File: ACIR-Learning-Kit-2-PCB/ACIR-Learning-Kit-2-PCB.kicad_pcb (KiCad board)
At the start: 2 copper layers, 297 x 210 mm, 39 parts, among them J1 1S 1P +ve, J10 1S 1P +ve, J11 1S 1P -ve, J12 1S 3P +ve, J13 1S 3P -ve, J14 1S 4P +ve, J15 1S 4P -ve, J16 1S 2P +ve, J17 1S 2P -ve, J18 1S 1P -ve, J19 2S 1P -ve, J2 1S 1P -ve, J20 3S 1P -ve, J3 4S B +ve, J4 4S B -ve, J5 4P B +ve, J6 4P B -ve, J7 2S 1P +ve, J8 3S 1P +ve, J9 4S 1P +ve

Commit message: feat: add PCB design files for ACIR Learning Kits 1 and 2
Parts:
- removed BT1: BH-18650-B5BA008, footprints:BH18650B1BA002
- removed J5: 4P B +ve, TestPoint:TestPoint_Pad_D2.0mm
- removed J6: 4P B -ve, TestPoint:TestPoint_Pad_D2.0mm
- added J21: 1S 1P +ve, TestPoint:TestPoint_Pad_D2.0mm, F.Cu at (169.1, 92.5)
- added J22: 1S 1P -ve, TestPoint:TestPoint_Pad_D2.0mm, F.Cu at (227.1, 92.5)
- added J23: 1S 1P +ve, TestPoint:TestPoint_Pad_D2.0mm, F.Cu at (183.3, 100.2)
- added J24: 1S 1P -ve, TestPoint:TestPoint_Pad_D2.0mm, F.Cu at (219.8, 100.2)
- moved J2 4.89 mm to (145.3, 82.4)
- moved J1 4.89 mm to (249.7, 82.4)
- turned BT7 to 180 degrees
- turned BT9 to 180 degrees
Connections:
- BT6 pad 1: /4P_B+ -> Net-(BT6-+)
- BT6 pad 2: /4P_B- -> Net-(BT6--)
- BT7 pad 1: /4P_B+ -> Net-(BT6--)
- BT7 pad 2: /4P_B- -> Net-(BT7--)
- BT8 pad 1: /4P_B+ -> Net-(BT7--)
- BT8 pad 2: /4P_B- -> Net-(BT8--)
- BT9 pad 1: /4P_B+ -> Net-(BT8--)
- BT9 pad 2: /4P_B- -> Net-(BT9--)
- J1 pad 1: /1S_B+ -> Net-(J1-Pin_1)
- J10 pad 1: /4P_B+ -> Net-(BT6-+)
- J11 pad 1: /4P_B- -> Net-(BT6--)
- J12 pad 1: /4P_B+ -> Net-(BT7--)
- J13 pad 1: /4P_B- -> Net-(BT8--)
- J14 pad 1: /4P_B+ -> Net-(BT9--)
- J15 pad 1: /4P_B- -> Net-(BT8--)
- J16 pad 1: /4P_B+ -> Net-(BT7--)
- J17 pad 1: /4P_B- -> Net-(BT6--)
- J2 pad 1: /1S_B- -> Net-(J1-Pin_1)
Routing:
- net /4P_B-: track 478.6 -> 0.00 mm, vias 797 -> 0
- net /4P_B+: track 478.6 -> 0.00 mm, vias 797 -> 0
- net Net-(J1-Pin_1): track 0.00 -> 208.7 mm, vias 0 -> 242
- net Net-(BT8--): track 0.00 -> 143.9 mm, vias 0 -> 266
- net Net-(BT6--): track 0.00 -> 143.9 mm, vias 0 -> 349
- net Net-(BT7--): track 0.00 -> 113.0 mm, vias 0 -> 319
- net /1S_B-: track 72.0 -> 0.00 mm, vias 121 -> 0
- net /1S_B+: track 72.0 -> 0.00 mm, vias 121 -> 0
- net Net-(BT9--): track 0.00 -> 72.0 mm, vias 0 -> 133
- net Net-(BT6-+): track 0.00 -> 72.0 mm, vias 0 -> 133
- net Net-(J21-Pin_1): track 0.00 -> 57.9 mm
- net Net-(J23-Pin_1): track 0.00 -> 36.4 mm
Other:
- board text added: "4S 1P - (I)"
- board text added: "4S 1P - (II)"
- board text added: "NOTE: In this section the Cells have diffrent ACIR The track Resistance are same but ACIR is diffrent because of the Cell Having Diffrent ACIR"
- board text added: "P1"
- board text added: "P2"
- board text added: "PCB Track Resistance"
- board text added: "Product ID: TST-ACR-V1.1-2607 Sub product ID: TST-ACR-V1.1-L2-2607 Version: V1.1"
- board text removed: "1S 1P"
- board text removed: "1S 4P"
- board text removed: "4S 1P"
- board text removed: "BT1"
- board text removed: "Product ID: TST-ACR-V1.1-2607 Sub product ID: TST-ACR-V1.1-L1-2607 Version: V1.1"

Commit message: feat: add ACIR Learning Kit 2 PCB design files and production outputs
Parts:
- renumbered J2 to P1, J1 to P2, J21 to P3, J22 to P4, J23 to P5, J24 to P6
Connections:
- J13 pad 1: Net-(BT8--) -> Net-(BT6--)
- J14 pad 1: Net-(BT9--) -> Net-(BT7--)
- J16 pad 1: Net-(BT7--) -> Net-(BT9--)
- J17 pad 1: Net-(BT6--) -> Net-(BT8--)
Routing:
- net Net-(BT6--): track 143.9 -> 270.9 mm, vias 349 -> 25
- net Net-(J21-Pin_1): track 57.9 -> 115.9 mm, vias 0 -> 118
- net Net-(BT8--): track 143.9 -> 95.7 mm, vias 266 -> 0
- net Net-(J23-Pin_1): track 36.4 -> 72.8 mm, vias 0 -> 74
- net Net-(BT7--): track 113.0 -> 95.7 mm, vias 319 -> 0
- net Net-(J1-Pin_1): vias 242 -> 226
- net Net-(BT9--): vias 133 -> 10
- net Net-(BT6-+): vias 133 -> 10
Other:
- board text added: "NOTE: In this section the Cells have same ACIR The track Resistance varies to demonstrate how interconnect trace impedance affects total pack ACIR"
- board text added: "P3"
- board text added: "P4"
- board text added: "P5"
- board text added: "P6"

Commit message: feat: DFM optimization - clean circular probing pads, uniform 2.0mm via pitch, and zero warnings
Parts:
- J10, J11, J12, J13, J14, J15, J16, J17, J18, J19, J20, J3, J4, J7, J8, J9, P1, P2, P3, P4, P5, P6: footprint TestPoint:TestPoint_Pad_D2.0mm -> footprints:TestPoint_Pad_D6.0mm
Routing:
- net /4S_B-: track 88.0 -> 76.0 mm, vias 121 -> 24
- net /4S_B+: track 88.0 -> 76.0 mm, vias 121 -> 24
- net Net-(J1-Pin_1): track 208.7 -> 200.4 mm, vias 226 -> 98
- net Net-(J23-Pin_1): track 72.8 -> 64.6 mm, vias 74 -> 30
- net Net-(J21-Pin_1): track 115.9 -> 107.7 mm, vias 118 -> 50
- net Net-(BT9--): track 72.0 -> 67.7 mm, vias 10 -> 24
- net Net-(BT6-+): track 72.0 -> 67.7 mm, vias 10 -> 24
- net Net-(BT6--): vias 25 -> 66
- net Net-(BT4--): vias 341 -> 66
- net Net-(BT3--): vias 336 -> 66
- net Net-(BT2--): vias 341 -> 66

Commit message: feat: synchronize Kit 2 silkscreen with Kit 1, achieve 100% parity, and update production deliverables
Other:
- board text added: "NOTE: In this section, cells have different ACIR values. Track resistance is constant to demonstrate how individual cell impedance affects total pack ACIR."
- board text added: "NOTE: In this section, cells have identical ACIR values. Track resistance varies to demonstrate how interconnect trace impedance affects total pack ACIR."
- board text added: "P10"
- board text added: "P11"
- board text added: "P12"
- board text added: "P13"
- board text added: "P14"
- board text added: "P15"
- board text added: "P16"
- board text added: "P17"
- board text added: "P18"
- board text added: "P7"
- board text added: "P8"
- board text added: "P9"
- board text removed: "BT2"
- board text removed: "BT3"
- board text removed: "BT4"
- board text removed: "BT5"
- board text removed: "BT6"
- board text removed: "BT7"
- board text removed: "BT8"
- board text removed: "BT9"
- board text removed: "NOTE: In this section the Cells have diffrent ACIR The track Resistance are same but ACIR is diffrent because of the Cell Having Diffrent ACIR"
- board text removed: "NOTE: In this section the Cells have same ACIR The track Resistance varies to demonstrate how interconnect trace impedance affects total pack ACIR"

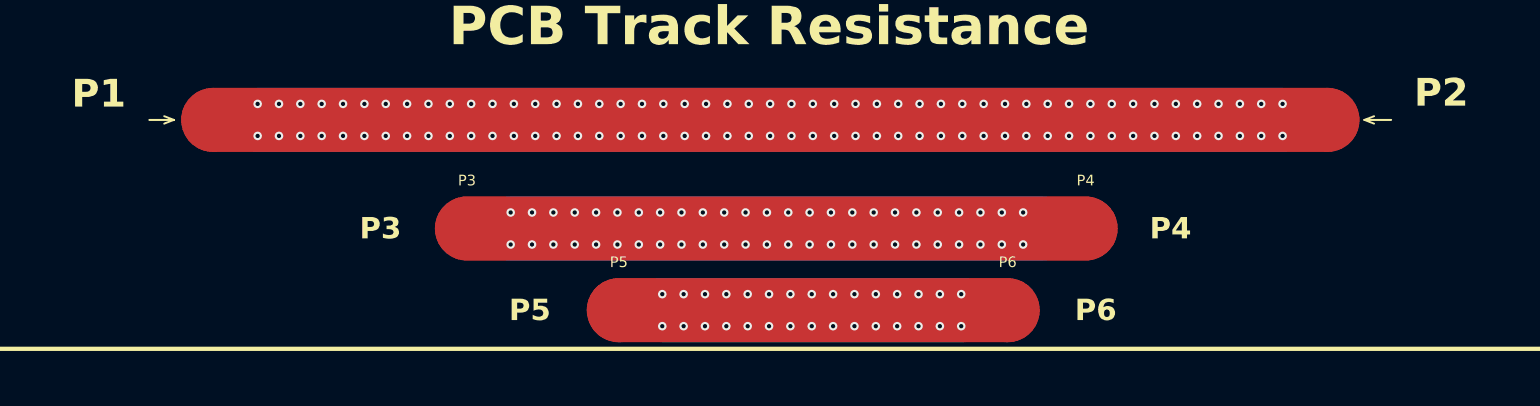
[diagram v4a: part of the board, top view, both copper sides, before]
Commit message: feat: make PCB Track Resistance equidistant, center-aligned, and symmetric with arrows for all probe points
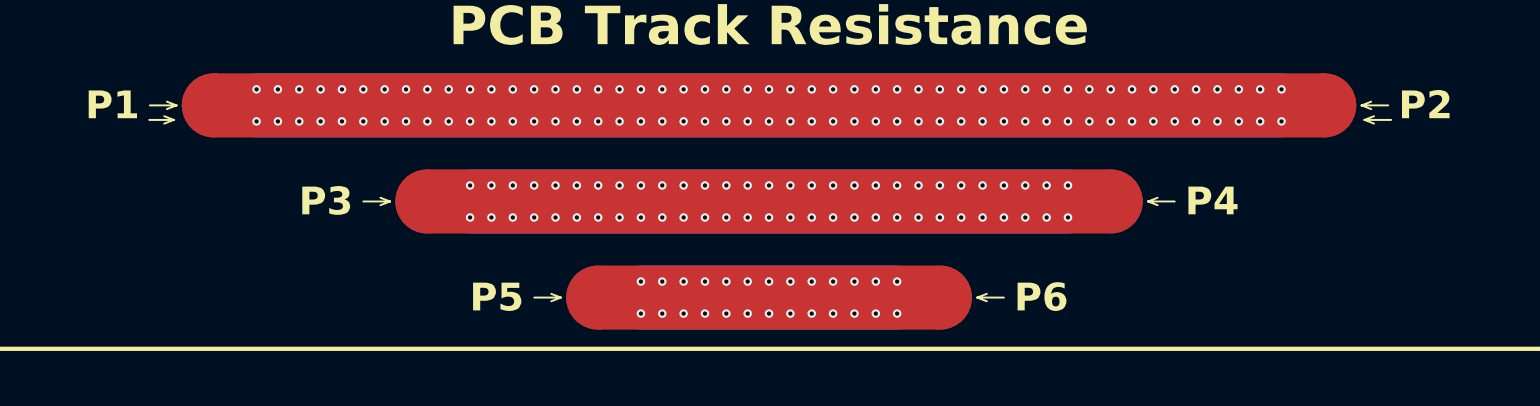
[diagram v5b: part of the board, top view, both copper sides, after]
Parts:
- moved P6 6.46 mm to (213.4, 99.0)
- moved P3 4.49 mm to (165.4, 90.0)
- moved P4 3.45 mm to (229.4, 90.0)
- moved P5 2.26 mm to (181.4, 99.0)
- moved P2 1.39 mm to (249.4, 81.0)
- moved P1 1.36 mm to (145.4, 81.0)
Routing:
- net Net-(J21-Pin_1): track 107.7 -> 120.0 mm, vias 50 -> 58
- net Net-(J23-Pin_1): track 64.6 -> 56.0 mm, vias 30 -> 26

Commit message: Restore battery holder solder pads and knockout polarity markings on Kit 2
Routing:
- net Net-(BT8--): track 95.7 -> 177.5 mm
- net Net-(BT7--): track 95.7 -> 177.5 mm
- net Net-(BT6-+): track 67.7 -> 61.5 mm

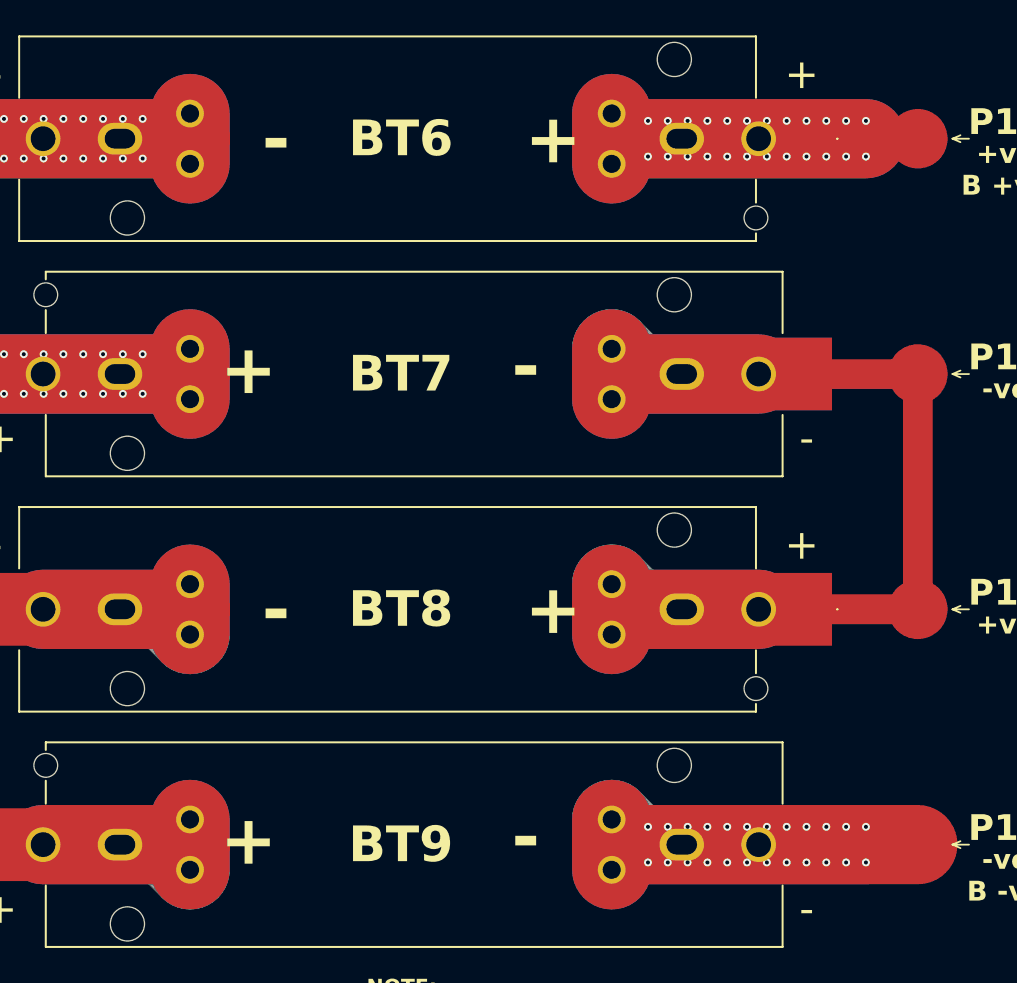
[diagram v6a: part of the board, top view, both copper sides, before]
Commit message: Standardize P18/P12 copper caps to match P10/P3 and add vias in 4S 1P (II)
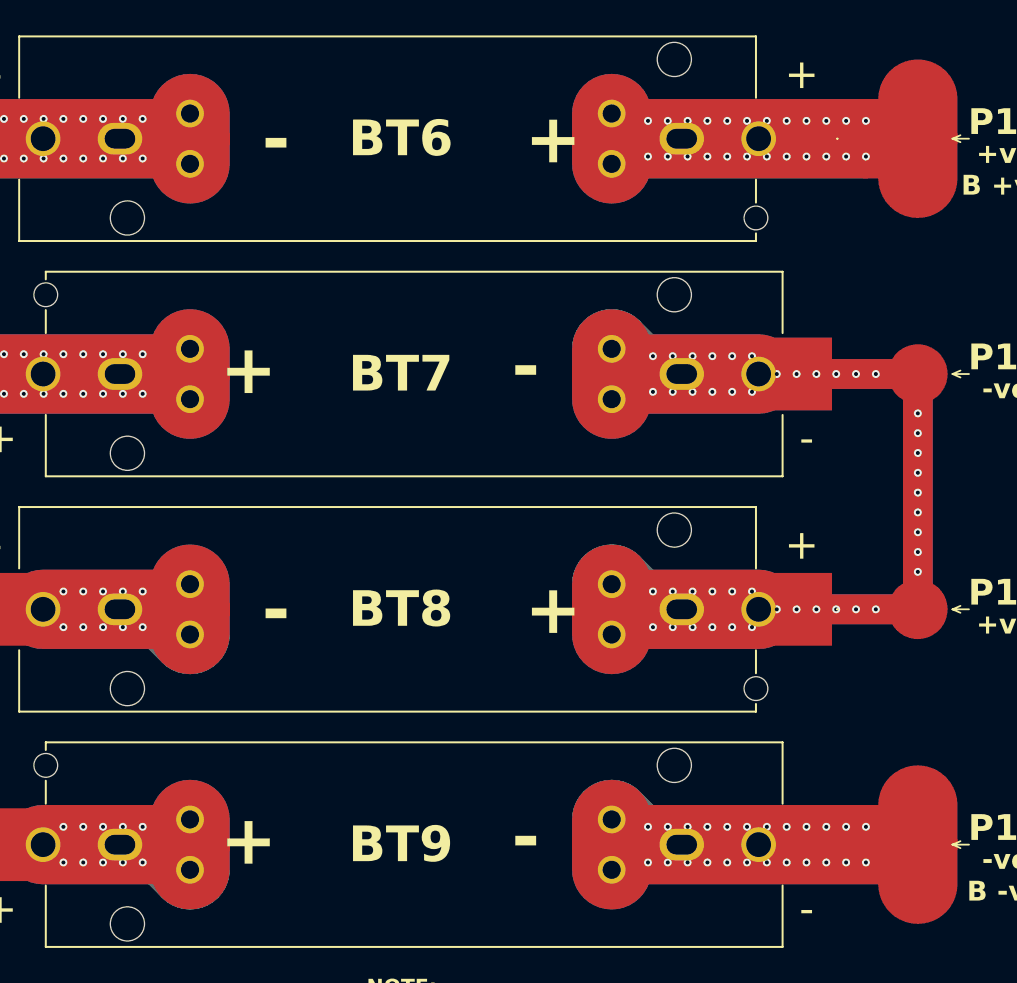
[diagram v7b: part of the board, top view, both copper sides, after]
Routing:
- net Net-(BT7--): track 177.5 -> 263.0 mm, vias 0 -> 45
- net Net-(BT6-+): track 61.5 -> 74.7 mm
- net Net-(BT9--): track 67.8 -> 75.8 mm
- net Net-(BT8--): vias 0 -> 20

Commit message: Remove vias overlapping battery holder solder pads across all cells
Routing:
- net Net-(BT9--): vias 24 -> 4
- net Net-(BT8--): vias 20 -> 0
- net Net-(BT7--): vias 45 -> 13
- net Net-(BT6--): vias 66 -> 26
- net Net-(BT6-+): vias 24 -> 4
- net Net-(BT4--): vias 66 -> 26
- net Net-(BT3--): vias 66 -> 26
- net Net-(BT2--): vias 66 -> 26
- net /4S_B-: vias 24 -> 4
- net /4S_B+: vias 24 -> 4
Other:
- board text added: "P19"
- board text added: "P20"
- board text added: "P21"
- board text added: "P22"
